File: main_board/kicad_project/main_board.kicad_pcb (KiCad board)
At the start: 4 copper layers, 150 x 120 mm, 244 parts, among them J1 MOTOR, J10 USB_B_Micro, J11 DATA_UART, J12 I2C_EXTERNAL, J13 DEBUG_HEADER, J14 IO1, J15 IO7, J16 IO2, J17 IO3, J18 IO8, J19 IO9, J2 MOTOR, J20 IO4, J21 IO5, J22 IO10, J23 IO6, J24 EXPANSION_HEADER, J3 MOTOR, J4 MOTOR, J5 PWR_ENTRY, J6 12V_HDR, J7 3V3_HDR, J8 5V_HDR, J9 I2C_BUFFERED, SW1 SW_SPST, U1 TMC2209, U2 TMC2209, U3 TMC2209, U4 TMC2209, U5 TPS562200, U6 TPS562200, U7 PCA9600DP, U8 USBLC6-2SC6, U9 STM32G474VxT, Y1 ABS06-32.768kHz, Y2 DNP

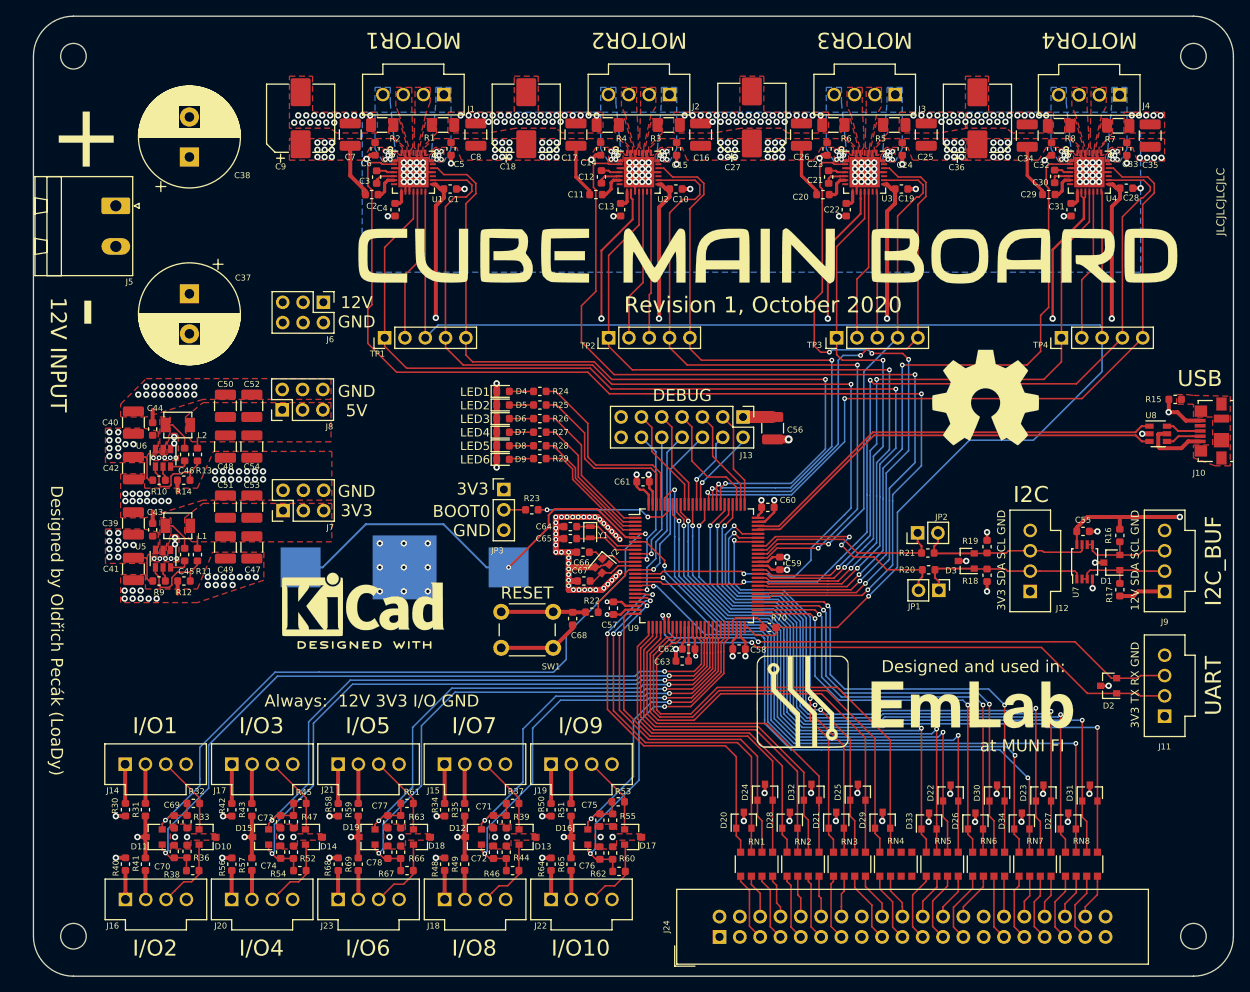
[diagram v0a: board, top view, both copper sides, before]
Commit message: change resistor network package
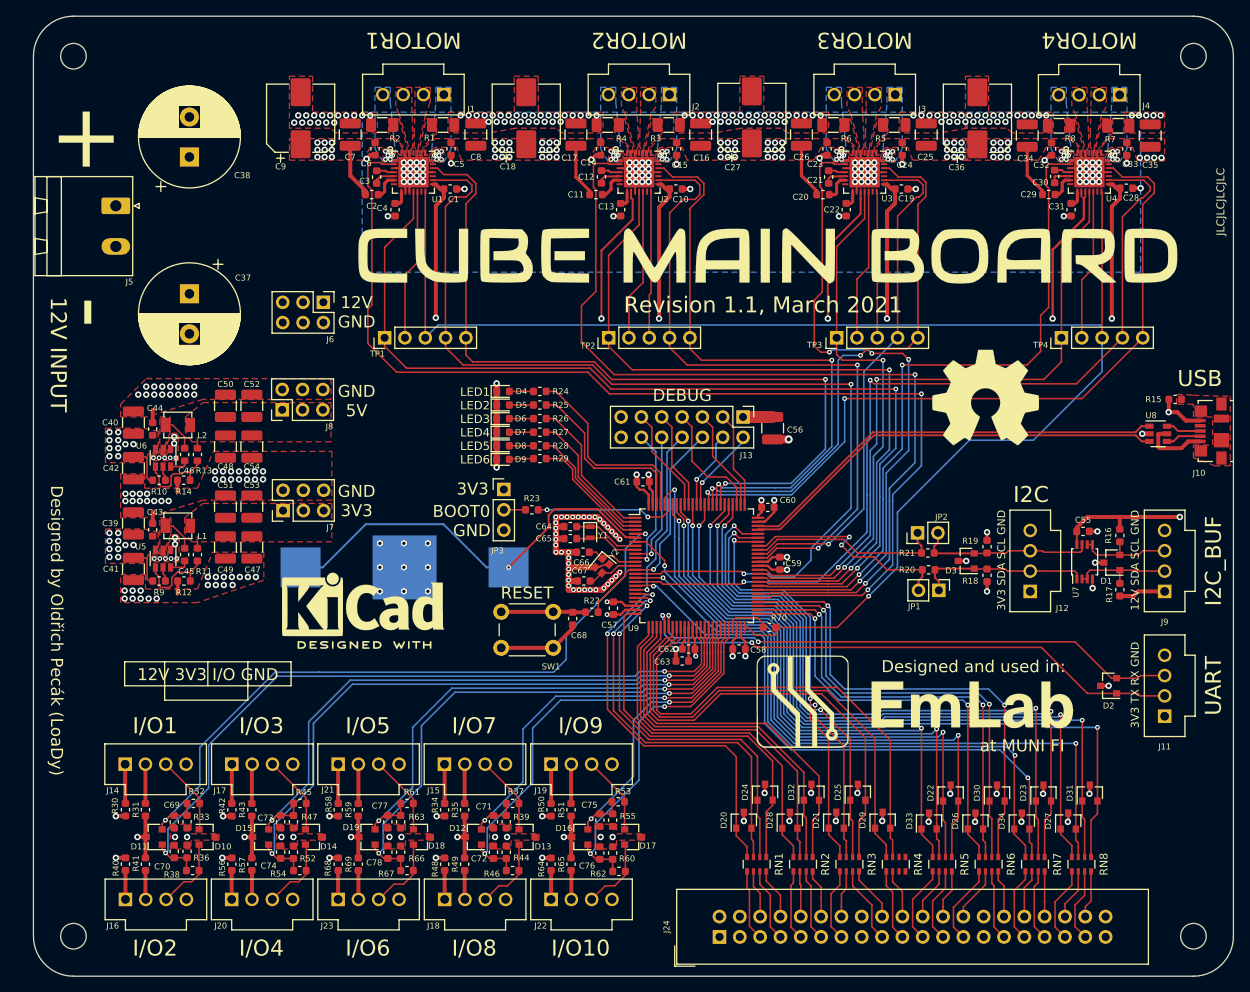
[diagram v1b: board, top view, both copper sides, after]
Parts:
- RN1, RN2, RN3, RN4, RN5, RN6, RN7, RN8: footprint Resistor_SMD:R_Array_Convex_4x1206 -> Resistor_SMD:R_Array_Convex_4x0603
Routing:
- net /MCU/EXP_IO5: track 43.6 -> 44.5 mm
- net /MCU/EXP_IO4: track 45.8 -> 46.8 mm
- net /MCU/EXP_IO23: track 75.3 -> 76.2 mm
- net /MCU/EXP_IO18: track 78.3 -> 79.2 mm
- net Net-(J24-Pad8): track 5.45 -> 6.39 mm
- net Net-(J24-Pad31): track 8.36 -> 9.29 mm
- net Net-(J24-Pad18): track 5.91 -> 6.84 mm
- net /MCU/EXP_IO22: track 59.4 -> 60.4 mm
- net /MCU/EXP_IO13: track 58.4 -> 59.3 mm
- net /MCU/EXP_IO12: track 57.4 -> 58.3 mm
- net Net-(J24-Pad21): track 8.81 -> 9.75 mm
- net /MCU/EXP_IO9: track 50.3 -> 51.2 mm
- net /MCU/EXP_IO30: track 89.5 -> 90.5 mm
- net /MCU/EXP_IO15: track 68.7 -> 69.6 mm
- net /MCU/EXP_IO1: track 50.2 -> 51.1 mm
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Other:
- board text added: "12V 3V3 I/O GND"
- board text added: "Cube Main Board Revision 1.1 Oldřich Pecák (LoaDy) Licensed under CERN-OHL-W v2 October 2020"
- board text added: "Revision 1.1, March 2021"
- board text removed: "Always: 12V 3V3 I/O GND"
- board text removed: "Cube Main Board Revision 1 Oldřich Pecák (LoaDy) Licensed under CERN-OHL-W v2 October 2020"
- board text removed: "Revision 1, October 2020"
